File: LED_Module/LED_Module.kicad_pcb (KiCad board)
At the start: 2 copper layers, 53.5 x 30 mm, 16 parts, among them P3 CONN_02X04, P4 CONN_02X04, U1 AL8805WS, U2 AL8805WS

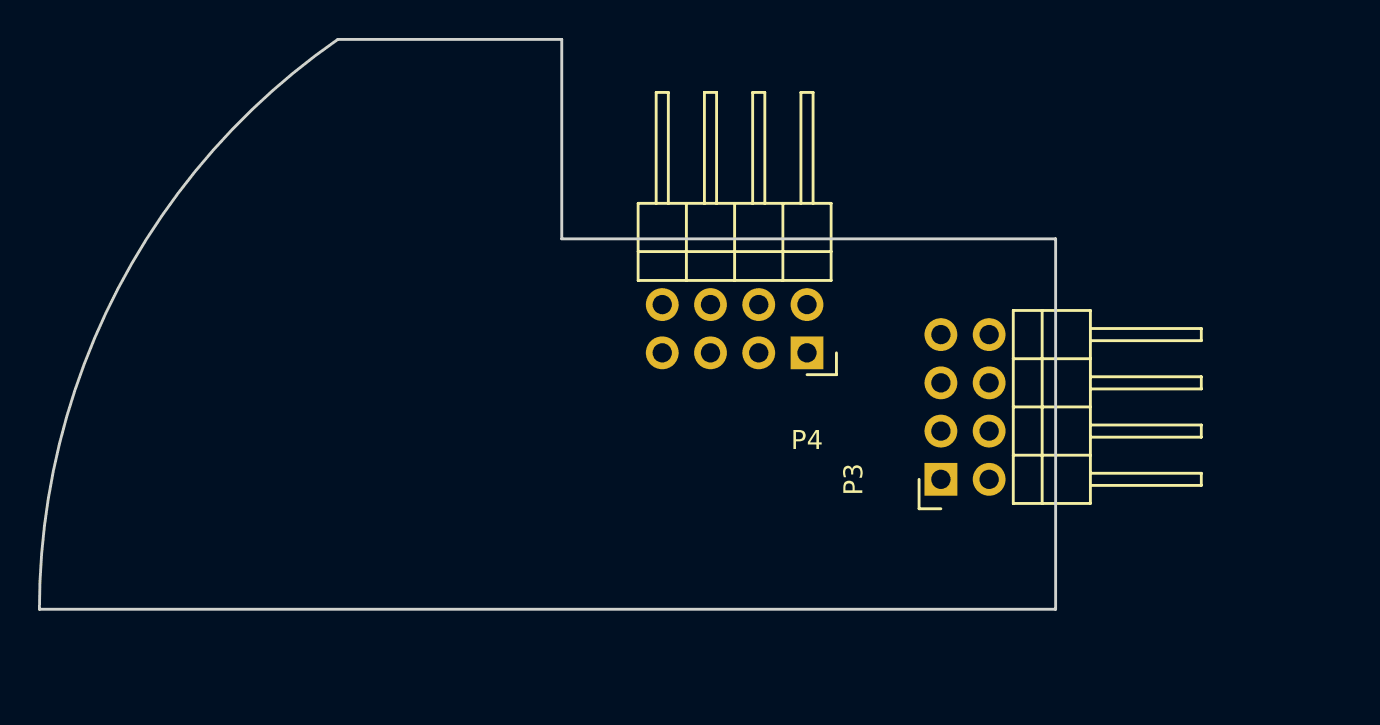
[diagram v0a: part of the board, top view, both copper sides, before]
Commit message: Resize PCBs
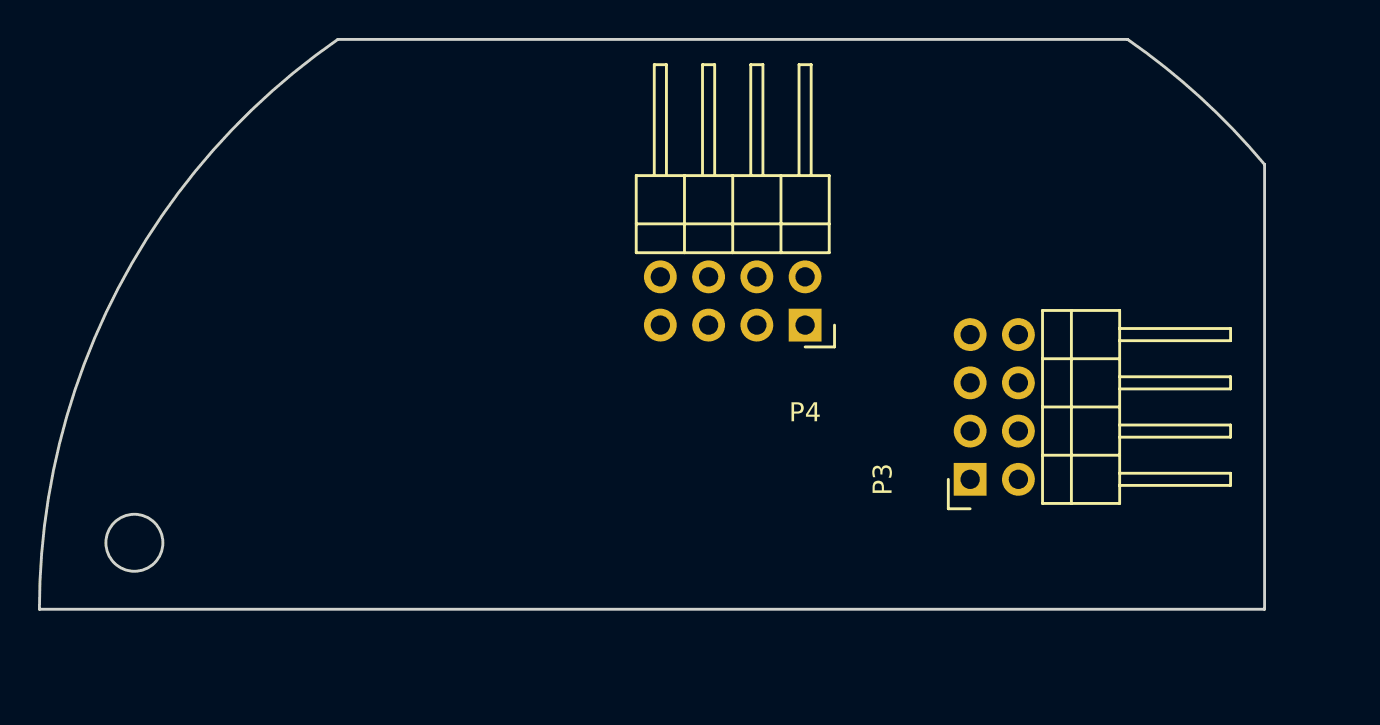
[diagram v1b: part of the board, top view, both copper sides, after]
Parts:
- moved P3 1.54 mm to (112.5, 93.2)
- moved P4 1.46 mm to (103.8, 85.0)
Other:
- board size 53.5 x 30 mm -> 64.5 x 30 mm
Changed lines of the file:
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@@
     (links 39)
     (no_connects 39)
-    (area 63.424999 69.924999 117.075001 100.075001)
+    (area 63.424999 69.924999 128.075001 100.075001)
     (thickness 1.6)
     (drawings 6)
@@
   )
   (module KiCad_Footprint:Socket_Strip_Angled_2x04 locked (layer F.Cu)
-    (at 103.91 86.5 180)
+    (at 103.81 85.04 180)
     (descr "Through hole socket strip")
     (tags "socket strip")
@@
   )
   (module KiCad_Footprint:Socket_Strip_Angled_2x04 locked (layer F.Cu)
-    (at 110.96 93.16 90)
+    (at 112.5 93.16 90)
     (descr "Through hole socket strip")
     (tags "socket strip")
@@
     )
   )
-  (gr_arc (start 100 100) (end 63.5 100) (angle 55.27723707) (layer Edge.Cuts) (width 0.15))
-  (gr_line (start 91 70) (end 79.209377 70) (layer Edge.Cuts) (width 0.15))
-  (gr_line (start 91 80.5) (end 91 70) (layer Edge.Cuts) (width 0.15))
-  (gr_line (start 117 80.5) (end 91 80.5) (layer Edge.Cuts) (width 0.15))
-  (gr_line (start 117 100) (end 117 80.5) (layer Edge.Cuts) (width 0.15))
-  (gr_line (start 117 100) (end 63.5 100) (layer Edge.Cuts) (width 0.15))
+  (gr_circle (center 68.5 96.5) (end 68.5 98) (layer Edge.Cuts) (width 0.15))
+  (gr_arc (start 100 100) (end 63.5 100) (angle 55.2772371) (layer Edge.Cuts) (width 0.15))
+  (gr_arc (start 100 100) (end 128 76.585261) (angle -15.3734978) (layer Edge.Cuts) (width 0.15))
+  (gr_line (start 120.790623 70) (end 79.209377 70) (layer Edge.Cuts) (width 0.15))
+  (gr_line (start 128 100) (end 128 76.585261) (layer Edge.Cuts) (width 0.15))
+  (gr_line (start 128 100) (end 63.5 100) (layer Edge.Cuts) (width 0.15))
 )

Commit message: Commit update
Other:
- outline, holes or cut-outs redrawn
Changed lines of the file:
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@@
     (links 39)
     (no_connects 39)
-    (area 63.424999 69.924999 128.075001 100.075001)
+    (area 63.424999 69.924999 169.230002 144.3)
     (thickness 1.6)
     (drawings 6)
@@
     )
   )
-  (gr_circle (center 68.5 96.5) (end 68.5 98) (layer Edge.Cuts) (width 0.15))
+  (gr_circle (center 67 96.5) (end 67 98) (layer Edge.Cuts) (width 0.15))
   (gr_arc (start 100 100) (end 63.5 100) (angle 55.2772371) (layer Edge.Cuts) (width 0.15))
   (gr_arc (start 100 100) (end 128 76.585261) (angle -15.3734978) (layer Edge.Cuts) (width 0.15))

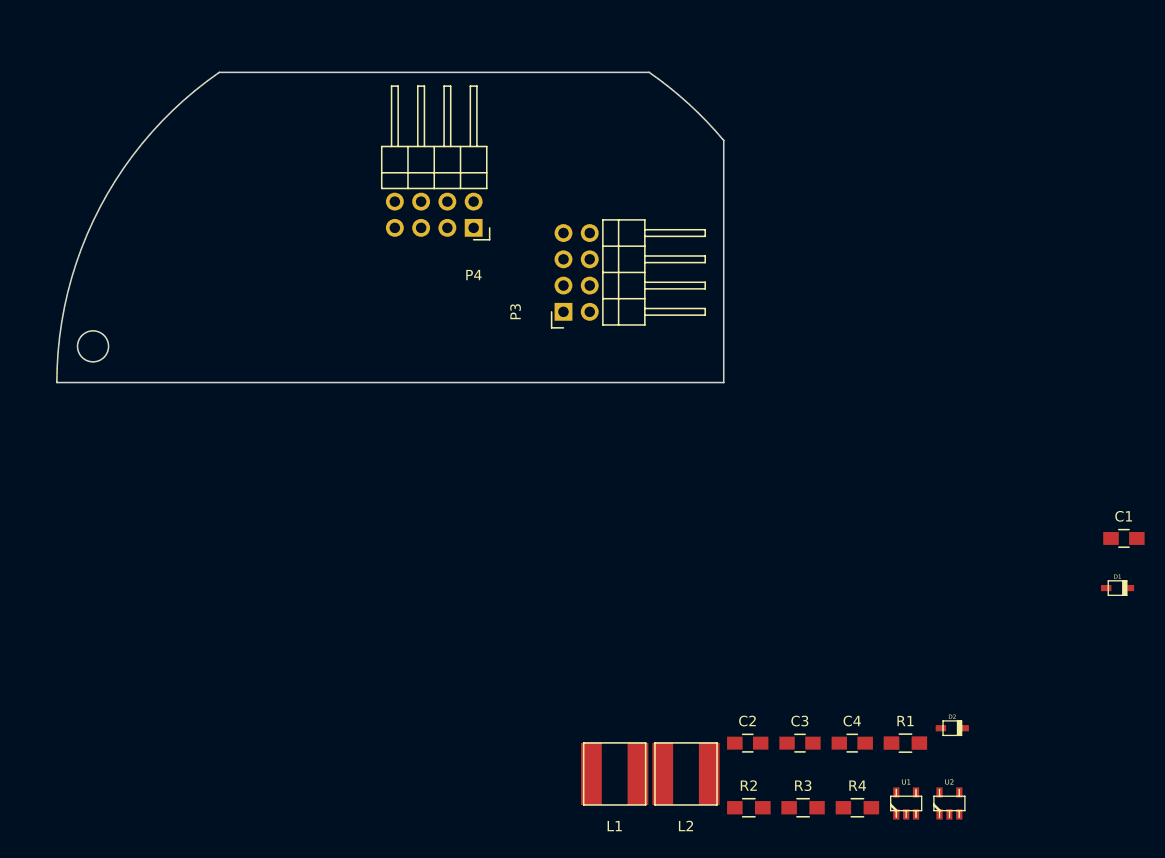
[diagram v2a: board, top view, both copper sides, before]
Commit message: Recover LED_Module project
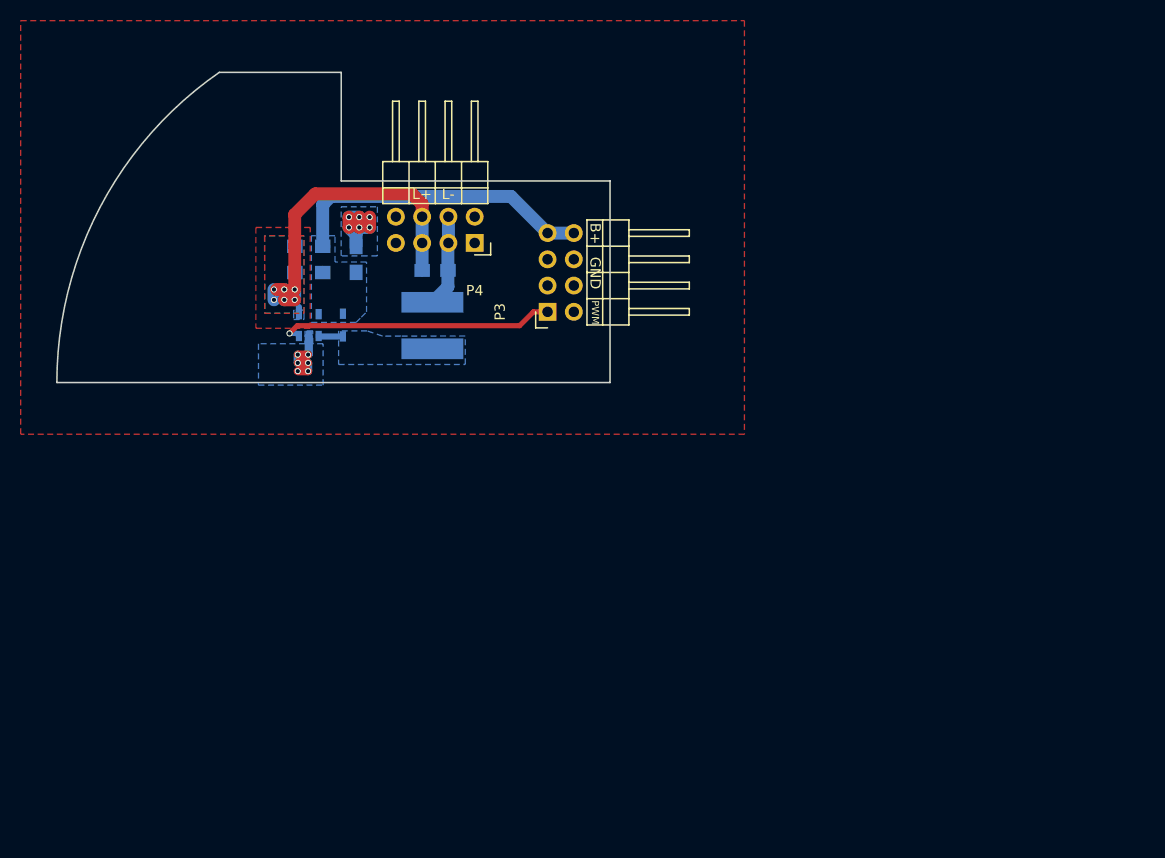
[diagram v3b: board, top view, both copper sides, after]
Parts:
- removed C2: 1uF, Capacitors_SMD:C_0805_HandSoldering
- removed C4: 2.2uF, Capacitors_SMD:C_0805_HandSoldering
- removed D2: BAT20JFILM, w_smd_diode:sod323
- removed L2: 33uH, inductor:inductor_33uH
- removed R2, R4: 0.5, Resistors_SMD:R_0805_HandSoldering
- removed U2: AL8805WS, w_smd_trans:sot23-5
- C1, C3, D1, L1, R1, R3, U1: moved to B.Cu
- moved D1 79.1 mm to (91.2, 94.4), turned to 270 degrees
- moved U1 74.0 mm to (87.9, 94.4), turned to 180 degrees
- moved R1 73.5 mm to (87.9, 89.4), turned to 180 degrees
- moved R3 72.4 mm to (87.9, 86.8), turned to 180 degrees
- moved C1 71.5 mm to (100.1, 89.2)
- moved C3 63.5 mm to (92.4, 88.1), turned to 270 degrees
- moved L1 46.8 mm to (99.8, 94.5), turned to 90 degrees
- moved P3 1.54 mm to (111.0, 93.2)
- moved P4 1.46 mm to (103.9, 86.5)
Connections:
- D1 pad 2: /LED1- -> Net-(D1-Pad2)
- L1 pad 1: Net-(L1-Pad1) -> Net-(D1-Pad2)
- P4 pad 1: /LED1+ -> (no net)
- P4 pad 2: /LED1+ -> (no net)
- P4 pad 5: /LED2+ -> /LED1+
- P4 pad 6: /LED2+ -> /LED1+
- P4 pad 7: /LED2- -> (no net)
- P4 pad 8: /LED2- -> (no net)
- U1 pad 1: Net-(L1-Pad1) -> Net-(D1-Pad2)
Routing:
- net /LED1+: track 0.00 -> 32.7 mm, vias 0 -> 6
- net /V_BAT: track 0.00 -> 30.2 mm
- net /CTRL_PWM: track 0.00 -> 26.8 mm, vias 0 -> 1
- net GND: track 0.00 -> 13.6 mm, vias 0 -> 12
- net /LED1-: track 0.00 -> 8.92 mm
- net Net-(D1-Pad2): track 0.00 -> 2.37 mm
- added copper zone on B.Cu, net /LED1+
- added copper zone on F.Cu, net /LED1+
- added copper zone on B.Cu, net /V_BAT
- added copper zone on B.Cu, net GND
- added copper zone on F.Cu, net GND
- added copper zone on B.Cu, net Net-(D1-Pad2)
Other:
- board size 64.5 x 30 mm -> 53.5 x 30 mm
- net class Default: trace_width 0.25 -> 0.6
- board text added: "B+"
- board text added: "GND"
- board text added: "L+"
- board text added: "L-"
- board text added: "PWM"

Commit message: LED Modulization
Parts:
- removed P4: CONN_02X04, KiCad_Footprint:Socket_Strip_Angled_2x04
- added C2: C, Capacitors_SMD:c_elec_5x4.5, B.Cu at (92.2, 95.8)
- added D2: LED, KiCad_Footprint:Power_LED, F.Cu at (100.0, 100.0)
- added P1: CONN_01X03, Connectors_JST:JST_XH_B03B-XH-A_03x2.50mm_Straight, B.Cu at (98.8, 93.0)
- added P2: CONN_01X01, Wire_Pads:SolderWirePad_single_1-2mmDrill, F.Cu at (90.5, 104.8)
- P3: value CONN_02X04 -> CONN_01X01; footprint KiCad_Footprint:Socket_Strip_Angled_2x04 -> Wire_Pads:SolderWirePad_single_1-2mmDrill
- moved R3 22.4 mm to (94.2, 108.2), turned to 270 degrees
- moved C1 21.8 mm to (100.2, 111.0)
- moved R1 20.8 mm to (96.5, 108.2), turned to 270 degrees
- moved U1 18.1 mm to (99.8, 108.0), turned to 270 degrees
- moved C3 16.7 mm to (95.5, 104.5), turned to 0 degrees
- moved D1 14.0 mm to (99.8, 105.5), turned to 0 degrees
- moved L1 12.9 mm to (107.2, 105.0), turned to 325 degrees
- moved P3 2.76 mm to (109.5, 95.5), turned to 0 degrees
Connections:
- P3 pad 1: /CTRL_PWM -> /LED1-
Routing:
- net /LED1+: track 32.7 -> 0.00 mm, vias 6 -> 0
- net /V_BAT: track 30.2 -> 0.00 mm
- net /CTRL_PWM: track 26.8 -> 0.00 mm, vias 1 -> 0
- net GND: track 13.6 -> 0.00 mm, vias 12 -> 0
- net /LED1-: track 8.92 -> 0.00 mm
- net Net-(D1-Pad2): track 2.37 -> 0.00 mm
- removed copper zone on B.Cu, net /LED1+
- removed copper zone on F.Cu, net /LED1+
- removed copper zone on B.Cu, net /V_BAT
- removed copper zone on B.Cu, net GND
- removed copper zone on F.Cu, net GND
- removed copper zone on B.Cu, net Net-(D1-Pad2)
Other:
- board size 53.5 x 30 mm -> 26 x 26 mm
- board text removed: "B+"
- board text removed: "GND"
- board text removed: "L+"
- board text removed: "L-"
- board text removed: "PWM"

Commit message: PCB square shape
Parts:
- removed D2: LED, KiCad_Footprint:Power_LED
- added P4: CONN_01X01, Socket_Strips:Socket_Strip_Straight_1x01, F.Cu at (88.5, 100.0)
- added P5: CONN_01X01, Socket_Strips:Socket_Strip_Straight_1x01, F.Cu at (111.5, 100.0)
- C3, D1, L1, R1, R3, U1: moved to F.Cu
- P1: value CONN_01X03 -> CONN_01X01; footprint Connectors_JST:JST_XH_B03B-XH-A_03x2.50mm_Straight -> Socket_Strips:Socket_Strip_Straight_1x01; moved to F.Cu
- P2, P3: footprint Wire_Pads:SolderWirePad_single_1-2mmDrill -> Socket_Strips:Socket_Strip_Straight_1x01
- moved P3 21.0 mm to (88.5, 95.0)
- moved P1 19.9 mm to (106.8, 111.2)
- moved C2 17.3 mm to (100.0, 111.2), turned to 0 degrees
- moved U1 12.6 mm to (96.0, 96.0), turned to 180 degrees
- moved D1 9.53 mm to (99.0, 96.0), turned to 90 degrees
- moved R1 8.92 mm to (94.8, 99.5), turned to 180 degrees
- moved P2 7.06 mm to (93.2, 111.2)
- moved R3 6.27 mm to (94.8, 102.0), turned to 180 degrees
- moved L1 5.96 mm to (104.0, 100.0), turned to 270 degrees
- moved C1 5.51 mm to (100.0, 105.5)
- moved C3 5.13 mm to (99.0, 100.8), turned to 90 degrees
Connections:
- P2 pad 1: /LED1+ -> /V_BAT
- P3 pad 1: /LED1- -> /CTRL_PWM
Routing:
- net GND: track 0.00 -> 18.8 mm, vias 0 -> 18
- net /LED1-: track 0.00 -> 14.6 mm
- net /LED1+: track 0.00 -> 14.6 mm
- net /CTRL_PWM: track 0.00 -> 6.57 mm
- net /V_BAT: track 0.00 -> 4.55 mm
- added copper zone on F.Cu, net /LED1+
- added copper zone on F.Cu, net /LED1-
- added copper zone on F.Cu, net /V_BAT
- added copper zone on B.Cu, net GND
- added copper zone on F.Cu, net GND
- added copper zone on F.Cu, net Net-(D1-Pad2)
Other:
- board size 26 x 26 mm -> 30 x 30 mm
- net class Default: trace_width 0.6 -> 0.5
- board text added: "GND"
- board text added: "LED+"
- board text added: "LED-"
- board text added: "PWM"
- board text added: "V+"

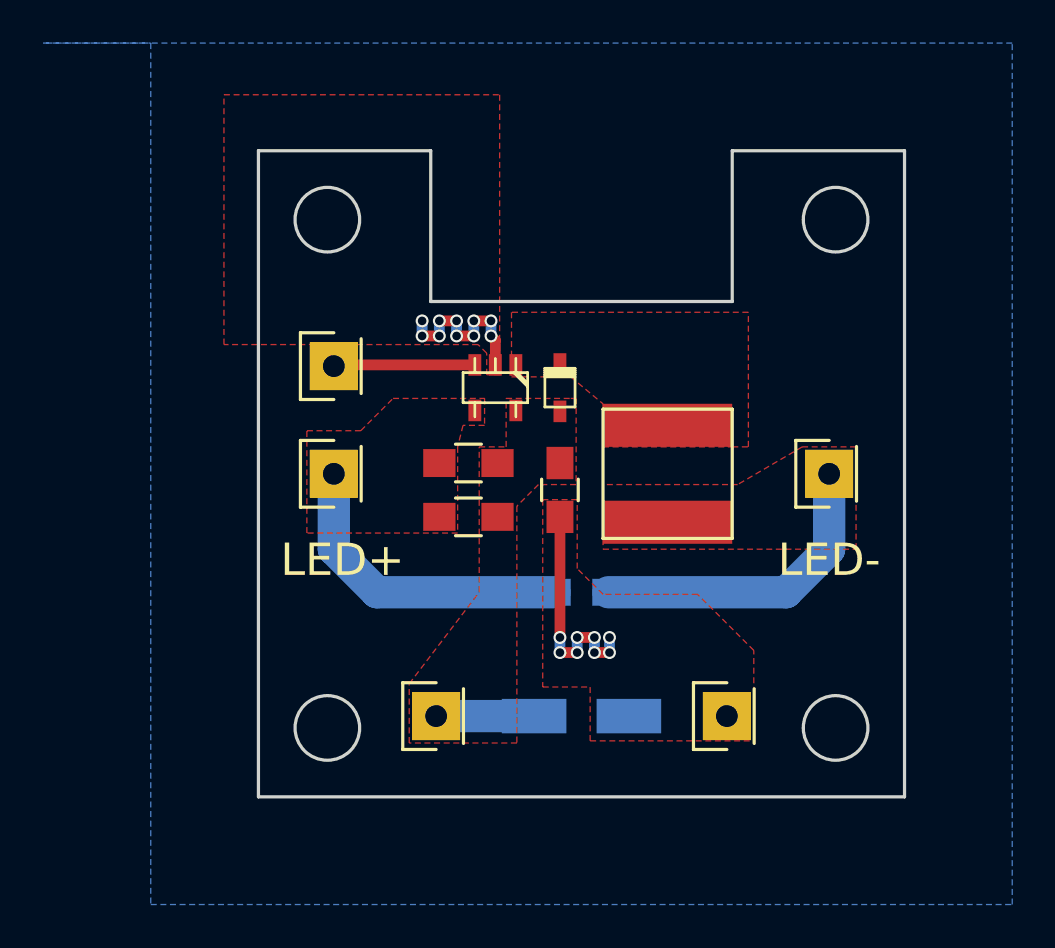
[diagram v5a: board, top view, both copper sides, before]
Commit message: Resize LED module
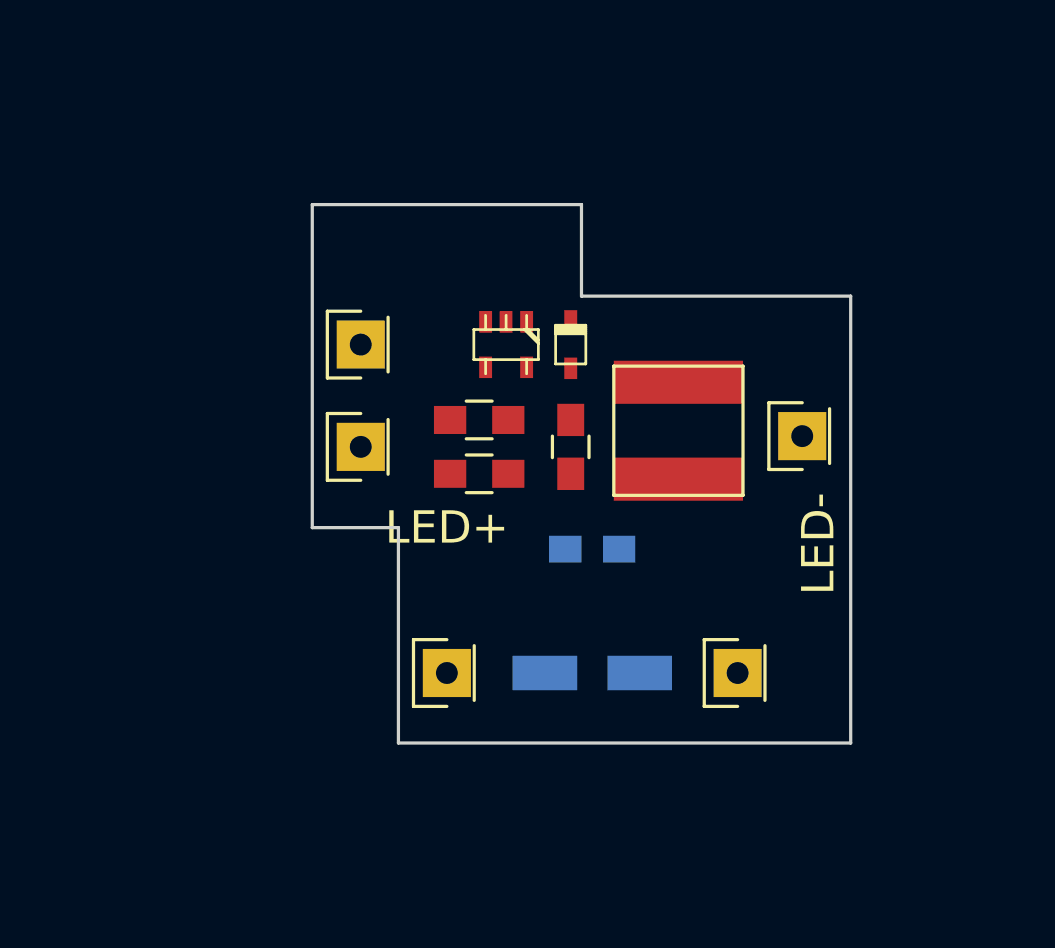
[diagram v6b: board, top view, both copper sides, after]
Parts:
- moved P5 2.15 mm to (110.2, 98.2)
- moved C1 2.06 mm to (100.5, 103.5)
- moved C2 2.06 mm to (100.5, 109.2)
- moved C3 2.06 mm to (99.5, 98.8)
- moved D1 2.06 mm to (99.5, 94.0)
- moved L1 2.06 mm to (104.5, 98.0)
- moved P1 2.06 mm to (107.2, 109.2)
- moved P2 2.06 mm to (93.8, 109.2)
- moved R1 2.06 mm to (95.2, 97.5)
- moved R3 2.06 mm to (95.2, 100.0)
- moved U1 2.06 mm to (96.5, 94.0)
- moved P4 1.77 mm to (89.8, 98.8)
- moved P3 1.60 mm to (89.8, 94.0)
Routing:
- net GND: track 18.8 -> 0.00 mm, vias 18 -> 0
- net /LED1-: track 14.6 -> 0.00 mm
- net /LED1+: track 14.6 -> 0.00 mm
- net /CTRL_PWM: track 6.57 -> 0.00 mm
- net /V_BAT: track 4.55 -> 0.00 mm
- removed copper zone on F.Cu, net /LED1+
- removed copper zone on F.Cu, net /LED1-
- removed copper zone on F.Cu, net /V_BAT
- removed copper zone on B.Cu, net GND
- removed copper zone on F.Cu, net GND
- removed copper zone on F.Cu, net Net-(D1-Pad2)
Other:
- board size 30 x 30 mm -> 25 x 25 mm
